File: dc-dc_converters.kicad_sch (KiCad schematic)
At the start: 58 parts, among them J3 JST_SH_1x4_SM04B-SRSS-TB-LF-SN, J4 Molex_Nano-Fit_1x2_105313-220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, U2 SIC477ED-T1-GE3, U3 AP62301WU-7, U4 AP62301WU-7

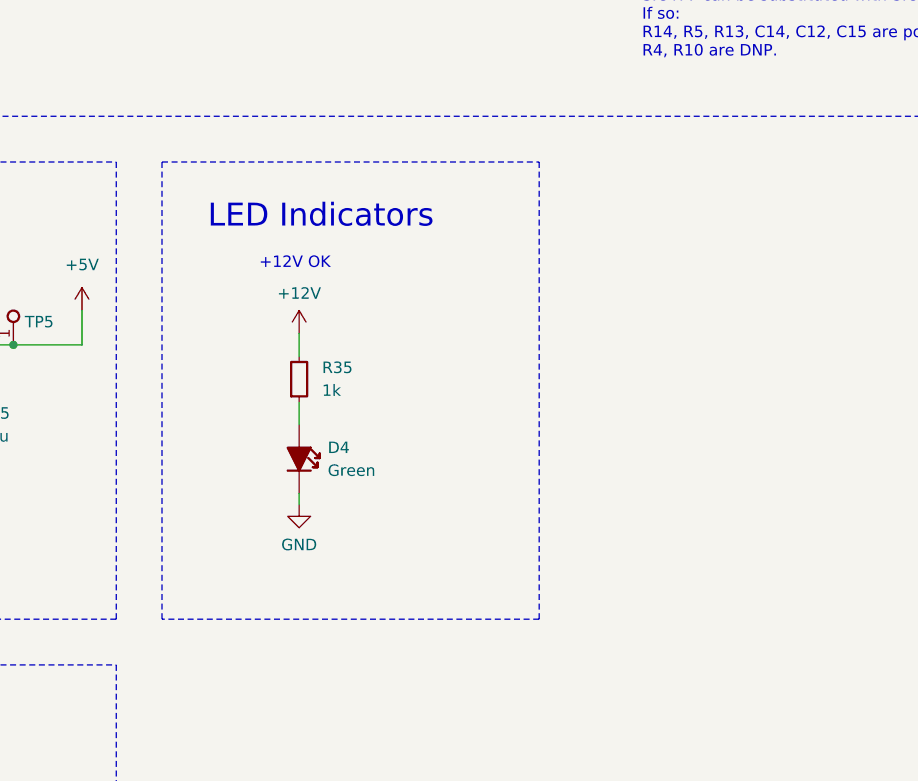
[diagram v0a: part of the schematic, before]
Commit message: [#57006] Add LEDs on 3v3 and 5v output
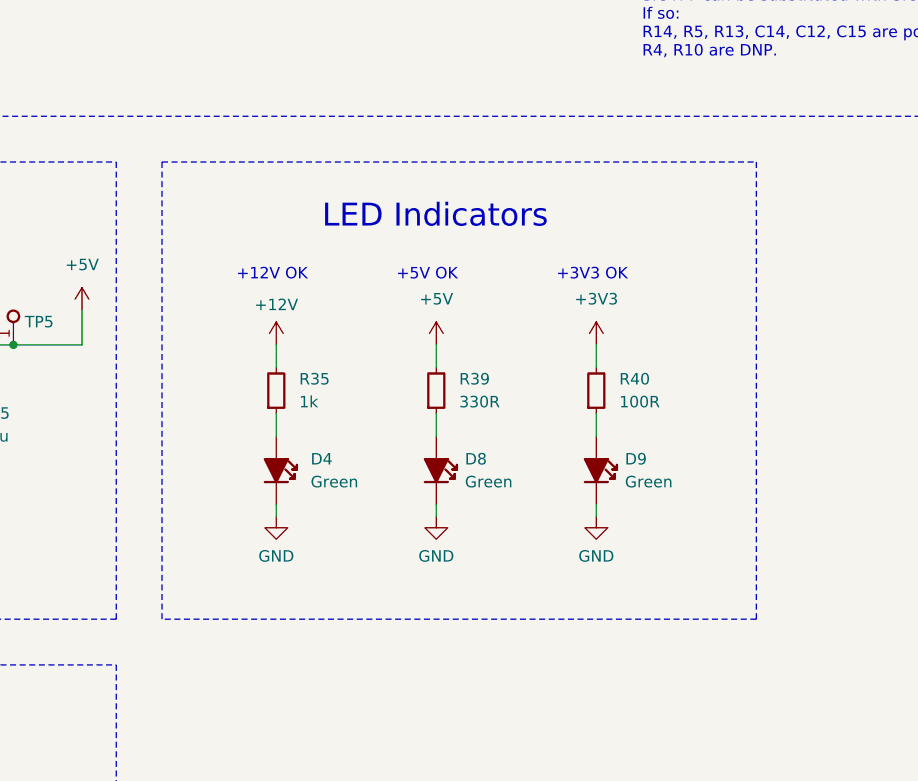
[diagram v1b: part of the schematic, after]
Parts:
- added D8, D9: LED_G_0603_LG_L29K-G2J1-24-Z, antmicro-footprints:LED_0603_1608Metric_G, symbol antmicroLEDIndicationDiscrete:LED_G_0603_LG_L29K-G2J1-24-Z
- added R39: R_330R_0402, antmicro-footprints:R_0402_1005Metric, symbol antmicroResistors0402:R_330R_0402
- added R40: R_100R_0402, antmicro-footprints:R_0402_1005Metric, symbol antmicroResistors0402:R_100R_0402
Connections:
- net +3V3: now also R40.2
- net +5V: now also R39.2
- net GND: now also D8.2, D9.2
- new net: D8.1, R39.1
- new net: D9.1, R40.1
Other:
- note added: "+3V3 OK"
- note added: "+5V OK"
- moved on the sheet: D4, R35

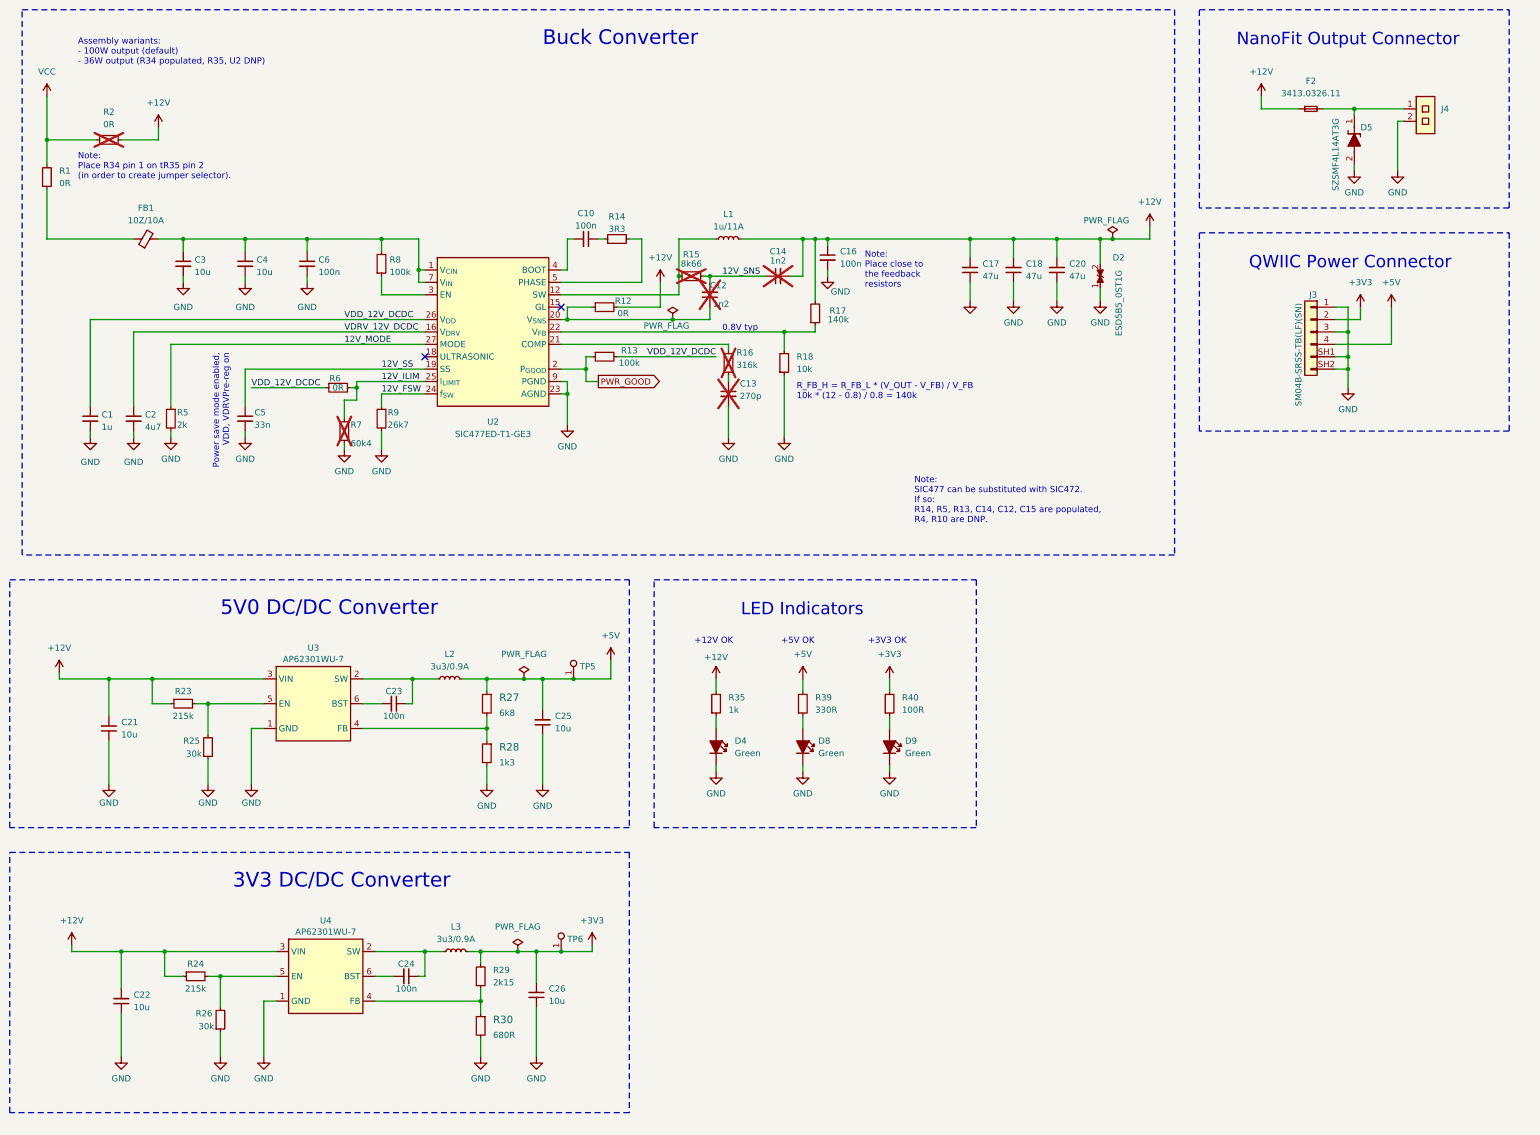
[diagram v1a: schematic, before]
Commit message: [#57006] Improve SIC472/SIC477 assembly variants note
Align components
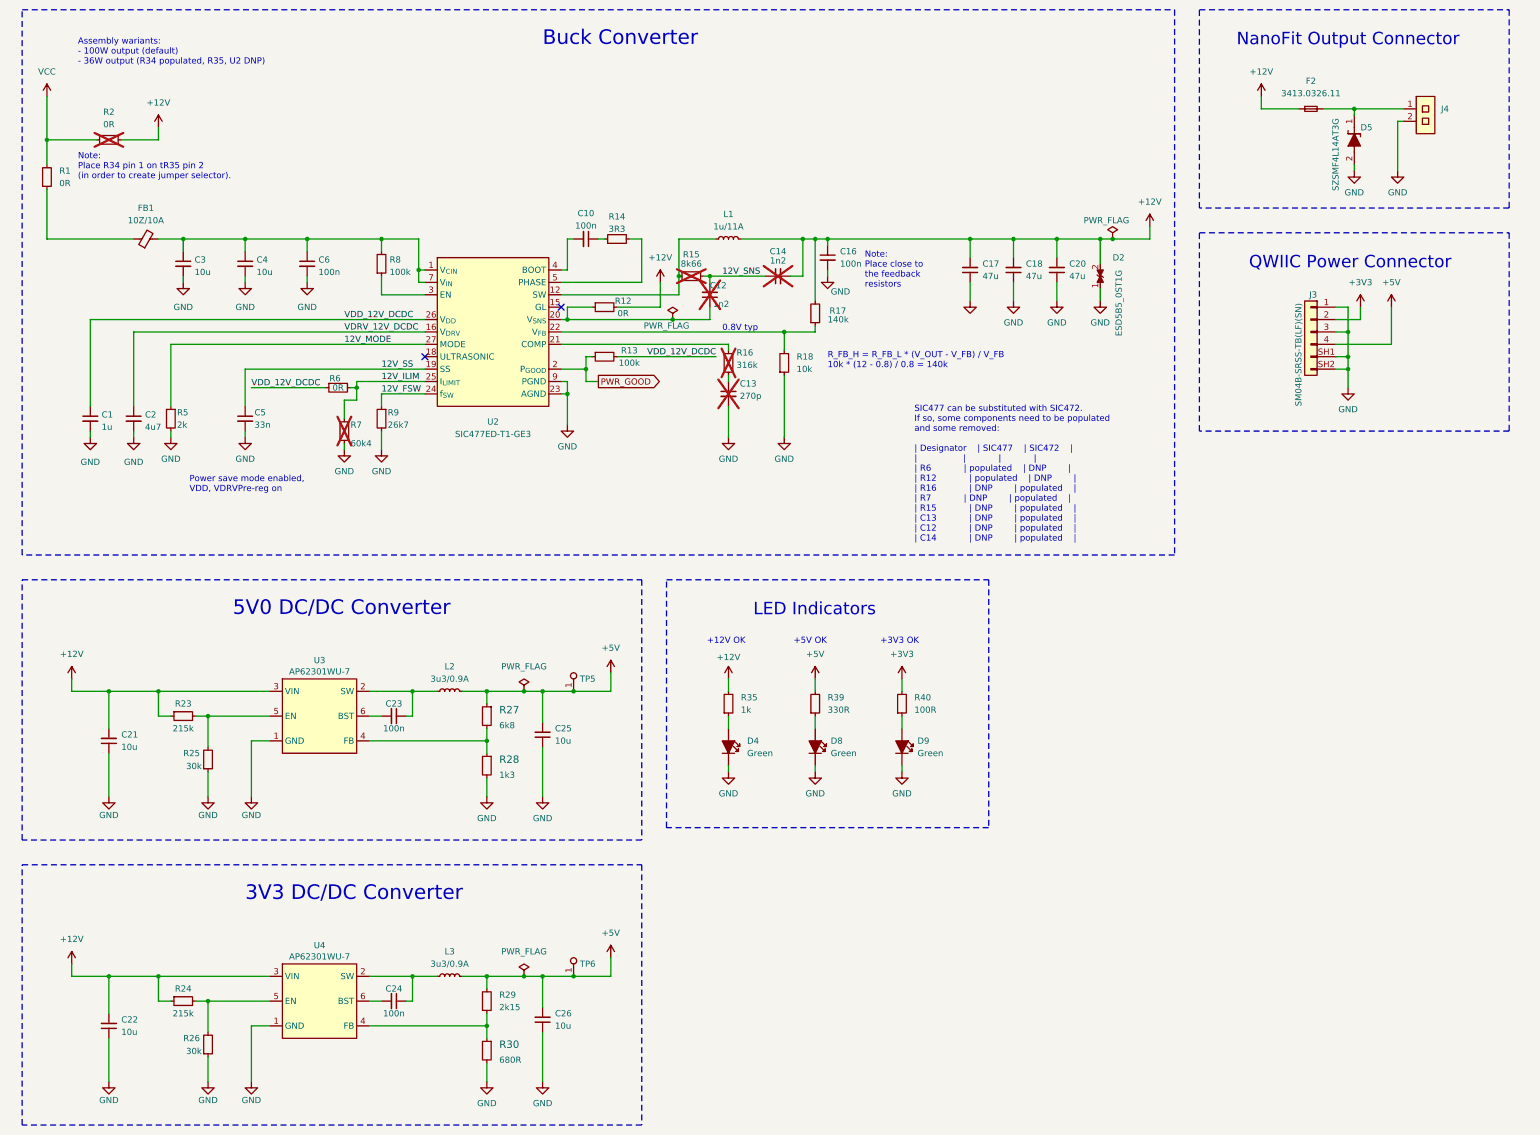
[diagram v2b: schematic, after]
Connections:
- net +3V3: no longer C26.2, L3.2, R29.2, TP6.1
- net +5V: now also C26.2, L3.2, R29.2, TP6.1
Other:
- note added: "SIC477 can be substituted with SIC472. If so, some components need to be populated and some removed: | Designator | SIC477 | SIC472 | | | | | | R6 | populated | DNP | | R12 | populated | DNP | | R16 | DNP | populated | | R7 | DNP | populated | | R15 | DNP | populated | | C13 | DNP | populated | | C12 | DNP | populated | | C14 | DNP | populated |"
- note removed: "Note: SIC477 can be substituted with SIC472. If so: R14, R5, R13, C14, C12, C15 are populated, R4, R10 are DNP."
- moved on the sheet: C21, C23, C25, D4, D8, D9, L2, R23, R25, R27, R28, R35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

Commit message: [#57006] Change power output variant selector
Use ferrites instead of resistors
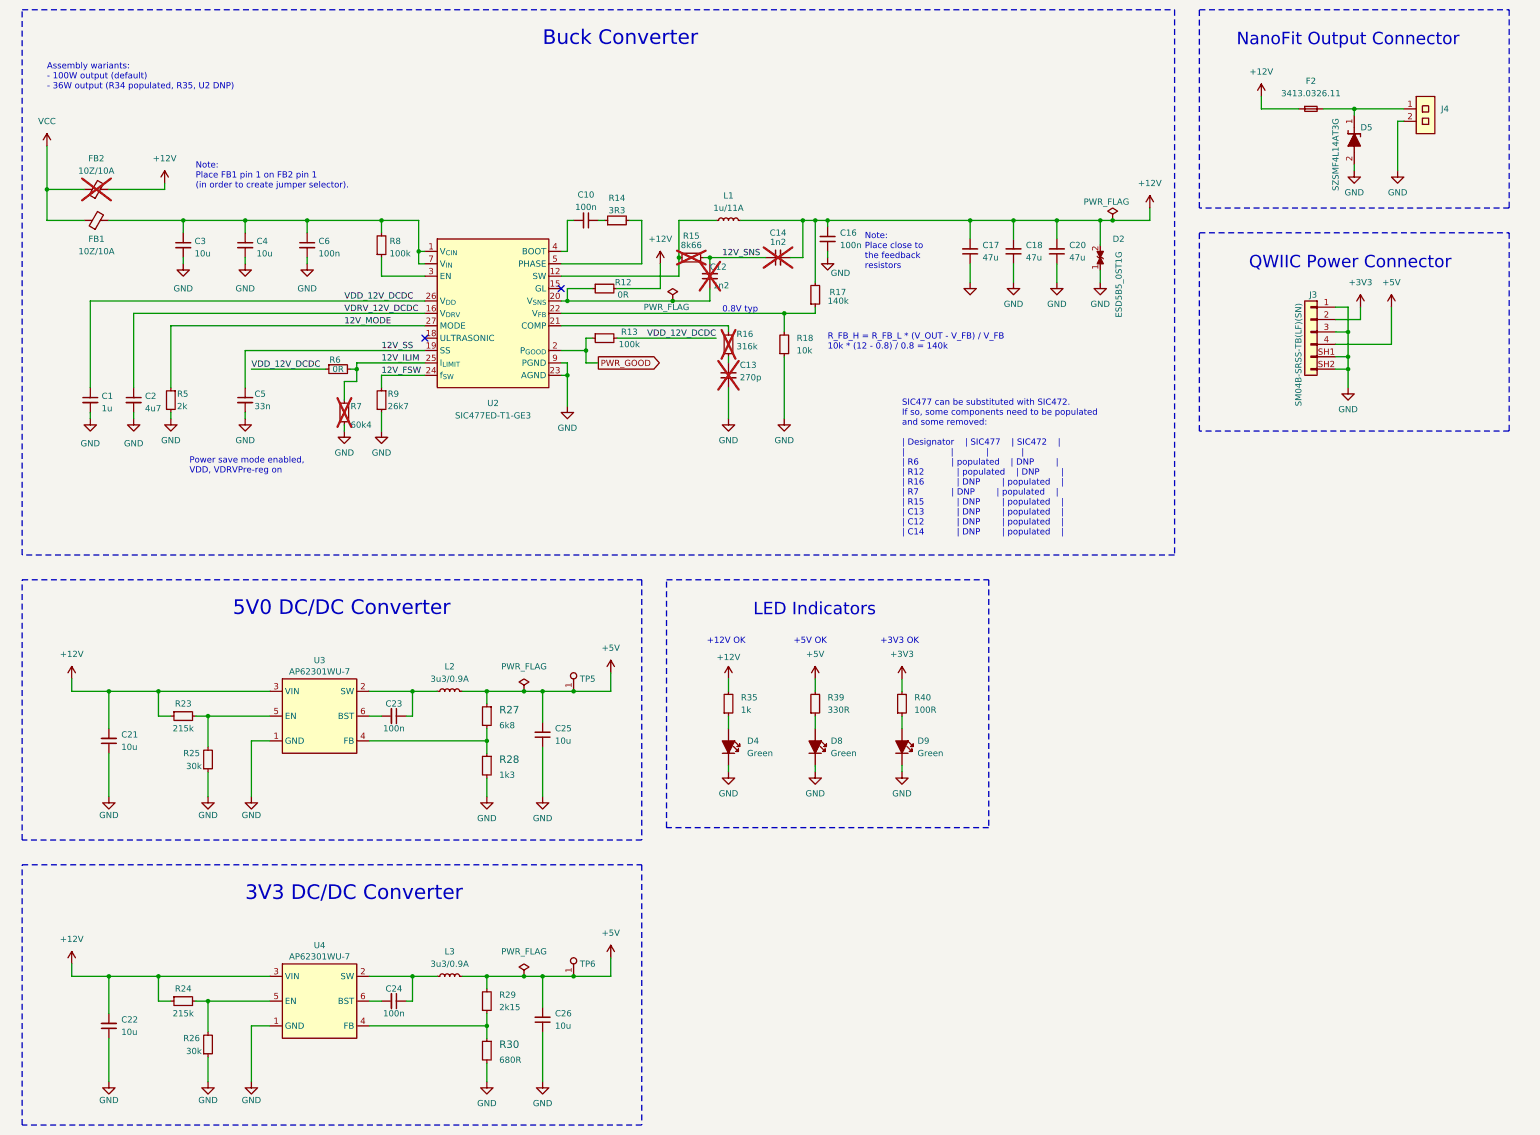
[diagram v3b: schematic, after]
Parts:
- removed R1, R2: R_0R_0805, antmicro-footprints:R_0805_2012Metric, symbol antmicroResistorsmisc:R_0R_0805
- added FB2: FB_10Z_10A_WE-MPSB_1206, antmicro-footprints:FB_1206_3216Metric, symbol antmicroFerriteBeadsandChips:FB_10Z_10A_WE-MPSB_1206
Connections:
- net +12V: now also FB2.2
- net VCC: now also FB1.1, FB2.1
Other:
- note added: "Note: Place FB1 pin 1 on FB2 pin 1 (in order to create jumper selector)."
- note removed: "Note: Place R34 pin 1 on tR35 pin 2 (in order to create jumper selector)."
- moved on the sheet: C1, C10, C12, C13, C14, C16, C17, C18, C2, C20, C3, C4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
